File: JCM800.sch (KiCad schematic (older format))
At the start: 111 parts, among them U1 ECC83, U2 ECC83, U3 ECC83, U4 EL84, U5 EL84

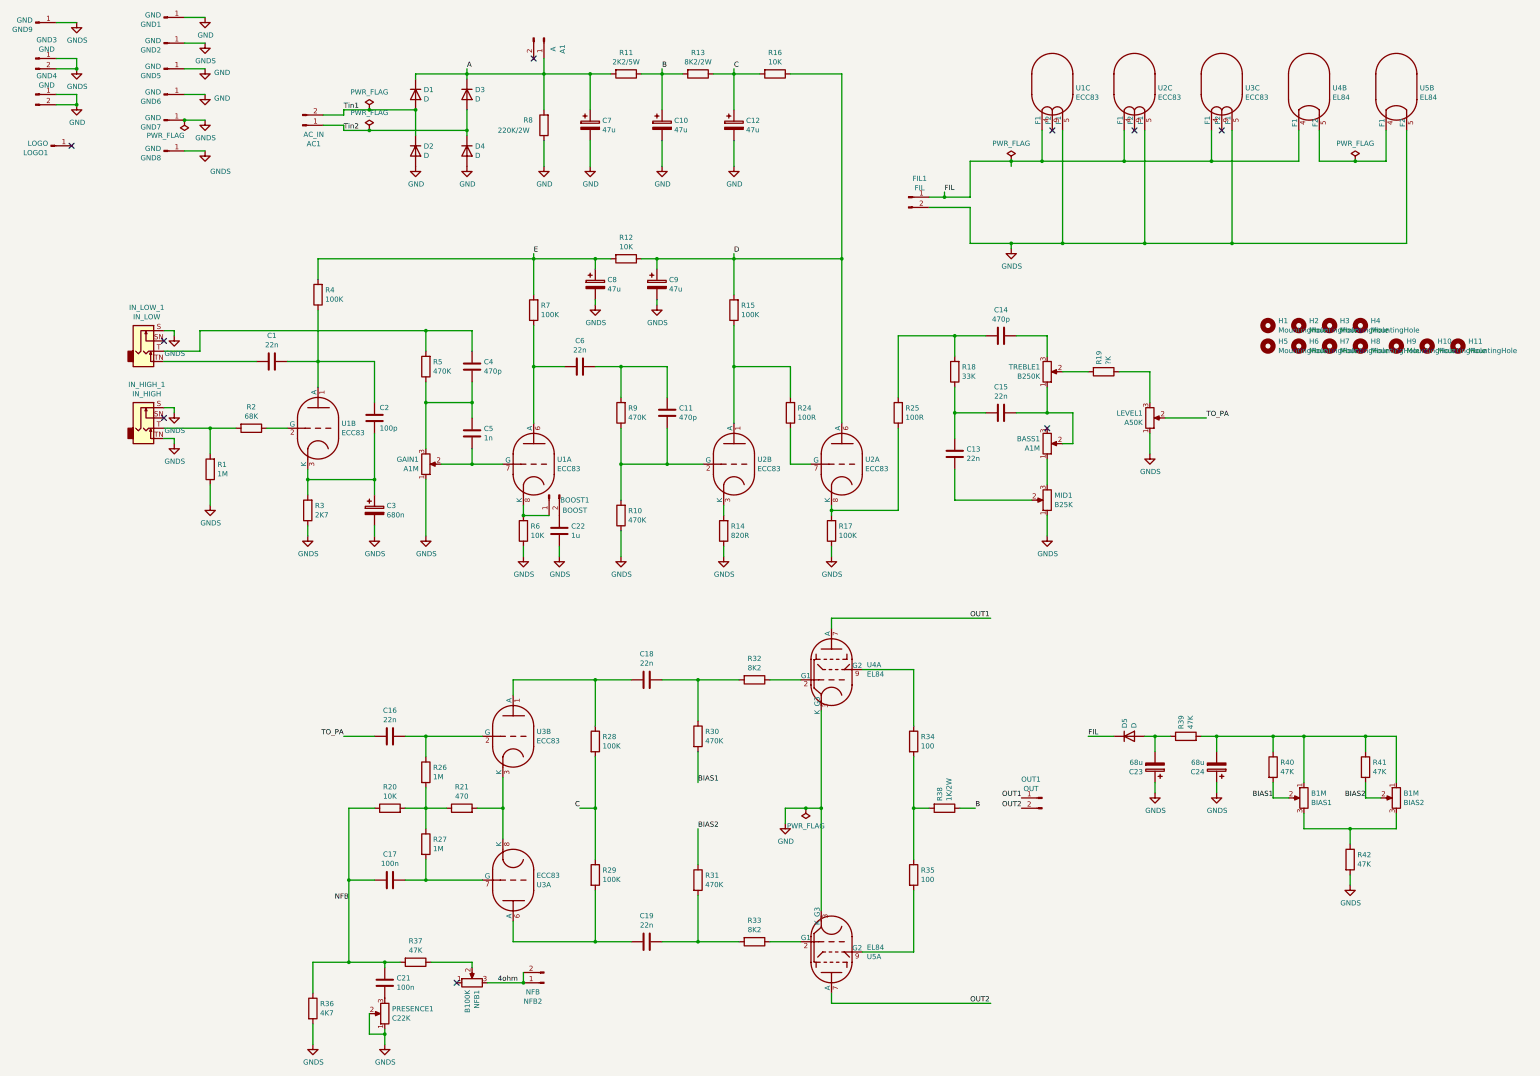
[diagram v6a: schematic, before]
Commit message: Test points added. Trimmers moved further away from pentode.
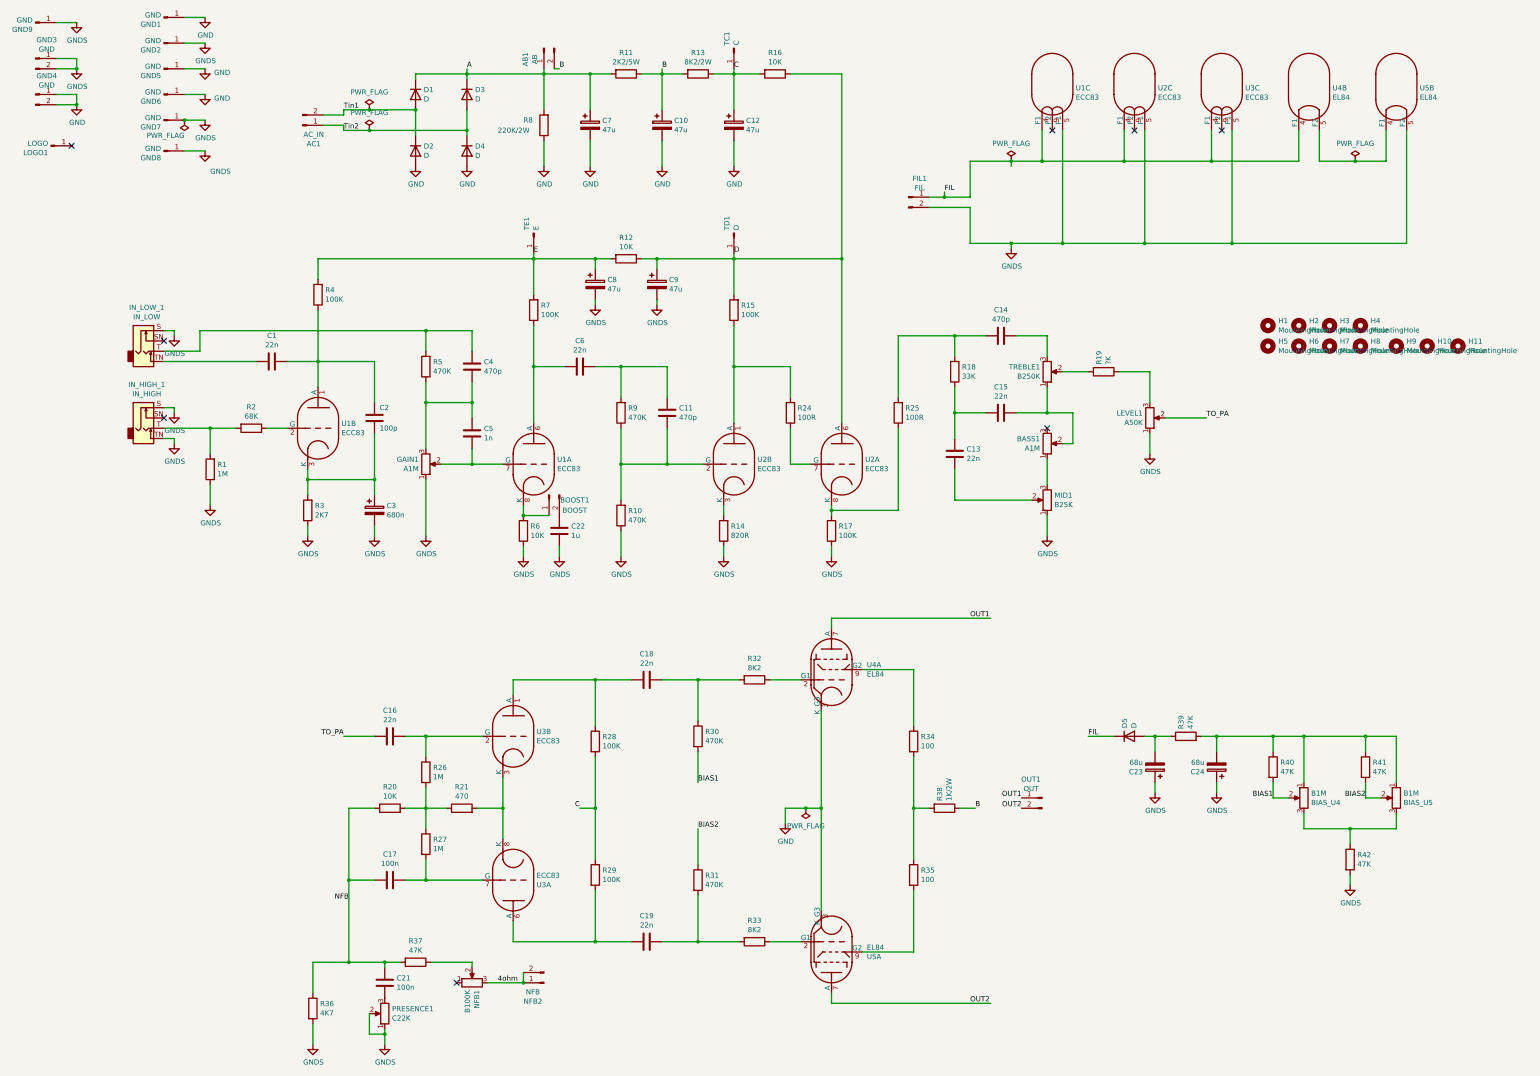
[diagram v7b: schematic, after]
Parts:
- added TC1: C, Connector_PinHeader_2.54mm:PinHeader_1x01_P2.54mm_Vertical, symbol Connector:Conn_01x01_Male
- added TD1: D, Connector_PinHeader_2.54mm:PinHeader_1x01_P2.54mm_Vertical, symbol Connector:Conn_01x01_Male
- added TE1: E, Connector_PinHeader_2.54mm:PinHeader_1x01_P2.54mm_Vertical, symbol Connector:Conn_01x01_Male
- AB1: renamed from A1; value A -> AB
- renumbered BIAS1 to BIAS_U4, BIAS2 to BIAS_U5
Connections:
- net B: now also AB1.2 (Pin_2)
- net C: now also TC1.1 (Pin_1)
- net D: now also TD1.1 (Pin_1)
- net E: now also TE1.1 (Pin_1)
- no-connect marks 9 -> 8
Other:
- moved on the sheet: AB1
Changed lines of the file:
@@
 encoding utf-8
 Sheet 1 1
-Title "JCM800 12W"
+Title "JCM800 15W"
 Date ""
 Rev "0.1"
@@
 Text Label 7750 1200 0    50   ~ 0
 C
-Wire Wire Line
-	7750 1200 7750 1250
 Text Label 7050 1200 0    50   ~ 0
 B
@@
 Wire Wire Line
 	10050 2550 10050 2900
-Wire Wire Line
-	7050 1200 7050 1250
 Text Label 7750 3000 0    50   ~ 0
 D
@@
 $EndComp
 $Comp
-L Connector:Conn_01x02_Male A1
+L Connector:Conn_01x02_Male AB1
 U 1 1 5DF591EA
-P 5900 900
-F 0 "A1" H 6008 1081 50  0000 C CNN
-F 1 "A" H 6008 990 50  0000 C CNN
-F 2 "TerminalBlock_MetzConnect:TerminalBlock_MetzConnect_Type094_RT03502HBLU_1x02_P5.00mm_Horizontal" H 5900 900 50  0001 C CNN
-F 3 "~" H 5900 900 50  0001 C CNN
-	1    5900 900
-	0    1    1    0
+P 5900 1000
+F 0 "AB1" H 6008 1181 50  0000 C CNN
+F 1 "AB" H 6008 1090 50  0000 C CNN
+F 2 "TerminalBlock_MetzConnect:TerminalBlock_MetzConnect_Type094_RT03502HBLU_1x02_P5.00mm_Horizontal" H 5900 1000 50  0001 C CNN
+F 3 "~" H 5900 1000 50  0001 C CNN
+	1    5900 1000
+	0    -1   1    0
 $EndComp
 $Comp
@@
 4ohm
 Wire Wire Line
-	5900 1100 5900 1250
-NoConn ~ 5800 1100
+	5900 1200 5900 1250
 $Comp
 L Connector:Conn_01x02_Male NFB2
@@
 Wire Wire Line
 	8250 8400 8250 8550
-Wire Wire Line
-	8600 8400 8450 8400
 Connection ~ 8600 8400
 Wire Wire Line
@@
 	14200 7700 14200 8150
 $Comp
-L Device:R_POT BIAS2
+L Device:R_POT BIAS_U5
 U 1 1 5E11ADDC
 P 14200 8300
-F 0 "BIAS2" H 14130 8254 50  0000 R CNN
+F 0 "BIAS_U5" H 14130 8254 50  0000 R CNN
 F 1 "B1M" H 14130 8345 50  0000 R CNN
 F 2 "Potentiometer_THT:Potentiometer_Bourns_3296W_Vertical" H 14200 8300 50  0001 C CNN
@@
 	13300 8150 13300 7700
 $Comp
-L Device:R_POT BIAS1
+L Device:R_POT BIAS_U4
 U 1 1 5E0F1978
 P 13300 8300
-F 0 "BIAS1" H 13230 8254 50  0000 R CNN
+F 0 "BIAS_U4" H 13230 8254 50  0000 R CNN
 F 1 "B1M" H 13230 8345 50  0000 R CNN
 F 2 "Potentiometer_THT:Potentiometer_Bourns_3296W_Vertical" H 13300 8300 50  0001 C CNN
@@
 	-1   0    0    1
 $EndComp
+Connection ~ 2400 1700
+Wire Wire Line
+	10800 5550 10800 5750
+Wire Wire Line
+	7750 1900 7750 2150
+$Comp
+L power:GND #GND0101
+U 1 1 5E4C2498
+P 2600 1200
+F 0 "#GND0101" H 2600 950 50  0001 C CNN
+F 1 "GND" H 2688 1163 50  0000 L CNN
+F 2 "" H 2600 1200 50  0001 C CNN
+F 3 "" H 2600 1200 50  0001 C CNN
+	1    2600 1200
+	1    0    0    -1
+$EndComp
+Connection ~ 6400 9700
+Connection ~ 4000 9100
+Wire Wire Line
+	4800 9900 5200 9900
+Wire Wire Line
+	5200 9900 5200 9950
+Wire Wire Line
+	4000 9100 4000 9900
+Wire Wire Line
+	4000 8400 4000 9100
+Wire Wire Line
+	7050 1200 7050 1250
+Wire Wire Line
+	7750 1200 7750 1250
+$Comp
+L Connector:Conn_01x01_Male TE1
+U 1 1 5DFCFD9D
+P 5800 2800
+F 0 "TE1" H 5772 2732 50  0000 R CNN
+F 1 "E" H 5772 2823 50  0000 R CNN
+F 2 "Connector_PinHeader_2.54mm:PinHeader_1x01_P2.54mm_Vertical" H 5800 2800 50  0001 C CNN
+F 3 "~" H 5800 2800 50  0001 C CNN
+	1    5800 2800
+	0    1    1    0
+$EndComp
+$Comp
+L Connector:Conn_01x01_Male TD1
+U 1 1 5DFD05BB
+P 7750 2800
+F 0 "TD1" H 7722 2732 50  0000 R CNN
+F 1 "D" H 7722 2823 50  0000 R CNN
+F 2 "Connector_PinHeader_2.54mm:PinHeader_1x01_P2.54mm_Vertical" H 7750 2800 50  0001 C CNN
+F 3 "~" H 7750 2800 50  0001 C CNN
+	1    7750 2800
+	0    1    1    0
+$EndComp
+$Comp
+L Connector:Conn_01x01_Male TC1
+U 1 1 5DFCF8A3
+P 7750 1000
+F 0 "TC1" H 7722 932 50  0000 R CNN
+F 1 "C" H 7722 1023 50  0000 R CNN
+F 2 "Connector_PinHeader_2.54mm:PinHeader_1x01_P2.54mm_Vertical" H 7750 1000 50  0001 C CNN
+F 3 "~" H 7750 1000 50  0001 C CNN
+	1    7750 1000
+	0    1    1    0
+$EndComp
+Wire Wire Line
+	6000 1200 6050 1200
+Text Label 6050 1200 0    50   ~ 0
+B
+Wire Wire Line
+	8450 8400 8250 8400
+Wire Wire Line
+	8600 8400 8450 8400
+Connection ~ 8450 8400
 $Comp
 L power:PWR_FLAG #FLG0103
@@
 	-1   0    0    1
 $EndComp
-Connection ~ 2400 1700
-Wire Wire Line
-	10800 5550 10800 5750
-Connection ~ 8450 8400
-Wire Wire Line
-	8450 8400 8250 8400
-Wire Wire Line
-	7750 1900 7750 2150
-$Comp
-L power:GND #GND0101
-U 1 1 5E4C2498
-P 2600 1200
-F 0 "#GND0101" H 2600 950 50  0001 C CNN
-F 1 "GND" H 2688 1163 50  0000 L CNN
-F 2 "" H 2600 1200 50  0001 C CNN
-F 3 "" H 2600 1200 50  0001 C CNN
-	1    2600 1200
-	1    0    0    -1
-$EndComp
-Connection ~ 6400 9700
-Connection ~ 4000 9100
-Wire Wire Line
-	4800 9900 5200 9900
-Wire Wire Line
-	5200 9900 5200 9950
-Wire Wire Line
-	4000 9100 4000 9900
-Wire Wire Line
-	4000 8400 4000 9100
 $EndSCHEMATC
